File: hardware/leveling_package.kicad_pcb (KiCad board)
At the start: 2 copper layers, 100 x 100 mm, 20 parts, among them J1 Conn_01x16_Male, J2 Conn_01x16_Male, J3 Conn_01x16_Male, J4 Conn_01x16_Male, Q1 BSS138, SW1 SW_Push

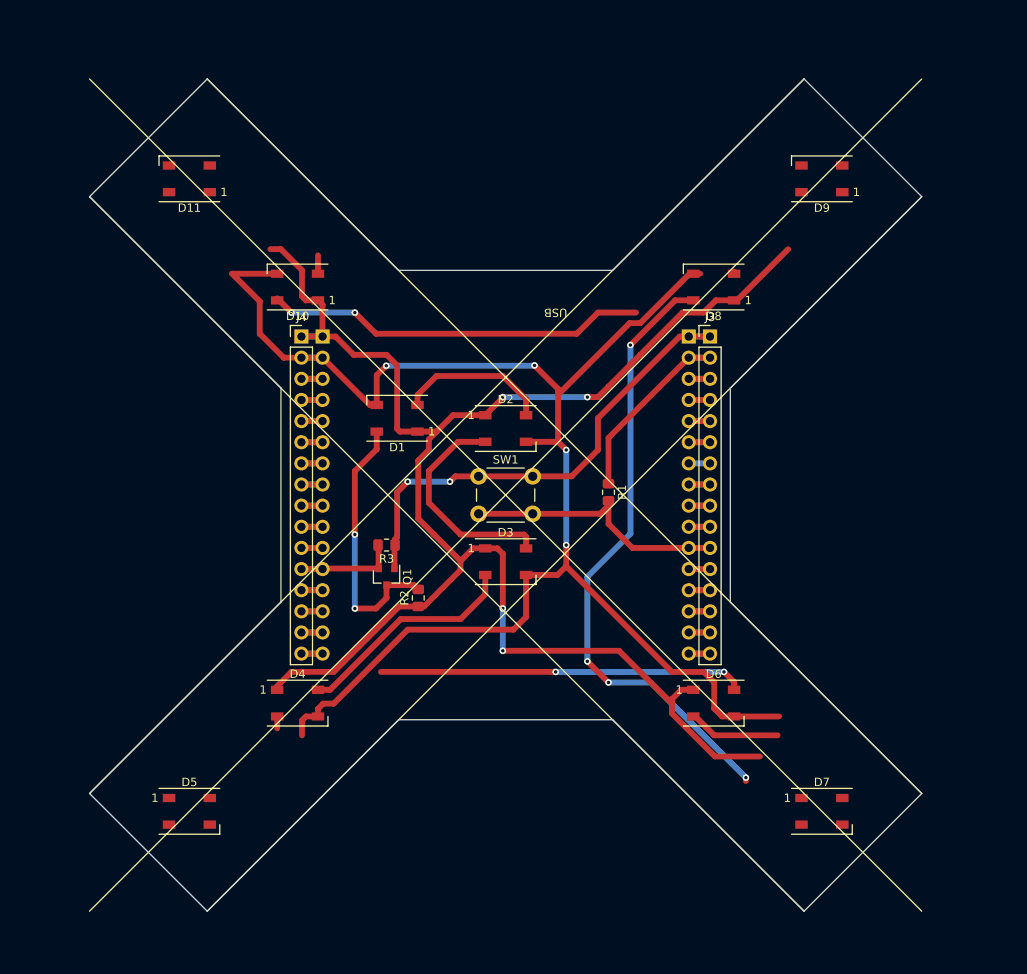
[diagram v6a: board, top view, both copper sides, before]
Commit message: all traces routed
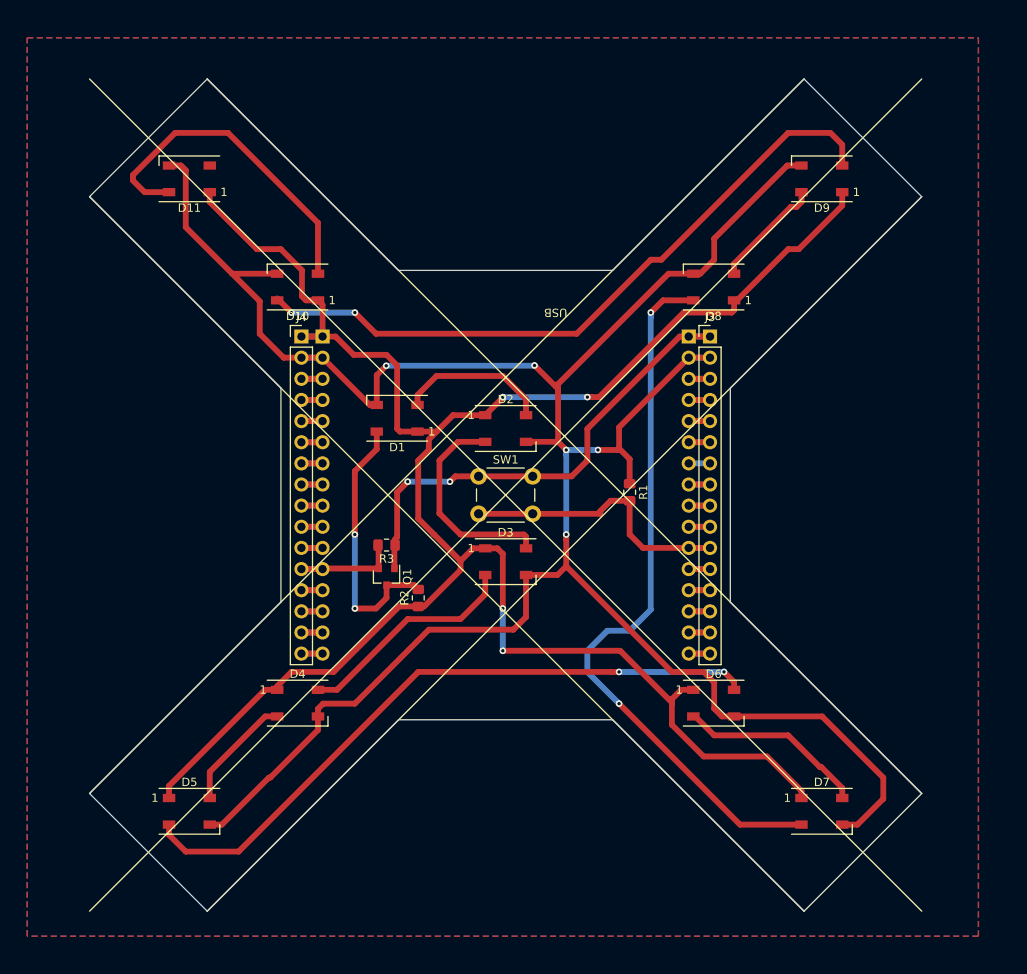
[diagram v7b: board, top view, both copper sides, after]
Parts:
- moved R1 2.54 mm to (88.9, 73.7)
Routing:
- net Net-(D1-Pad3): track 213.7 -> 296.6 mm, vias 4 -> 5
- net Net-(D1-Pad1): track 200.8 -> 250.2 mm
- net Net-(D10-Pad2): track 2.21 -> 40.5 mm
- net Net-(D10-Pad4): track 46.1 -> 82.9 mm
- net Net-(D5-Pad2): track 44.0 -> 80.5 mm
- net Net-(D8-Pad2): track 0.26 -> 13.8 mm
- net Net-(D4-Pad2): track 1.44 -> 14.0 mm
- net Net-(D7-Pad2): track 75.2 -> 87.0 mm, vias 4 -> 2
- net Net-(D6-Pad2): track 11.1 -> 22.7 mm
- net Net-(D2-Pad2): track 26.8 -> 25.8 mm
- net Net-(J1-Pad11): track 35.3 -> 35.9 mm
- added copper zone on B.Cu, net Net-(D1-Pad3)
- added copper zone on F.Cu, net Net-(D1-Pad3)

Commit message: minor corrections
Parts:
- moved D1 2.54 mm to (58.4, 64.8)
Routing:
- net Net-(D1-Pad2): track 18.3 -> 19.7 mm
- net Net-(D1-Pad3): track 296.6 -> 295.2 mm
- net Net-(D1-Pad4): track 32.2 -> 31.2 mm
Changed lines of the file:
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@@
   )
   (module LED_SMD:LED_WS2812B_PLCC4_5.0x5.0mm_P3.2mm (layer F.Cu)
-    (at 60.96 64.77 180)
+    (at 58.42 64.77 180)
     (descr https://cdn-shop.adafruit.com/datasheets/WS2812B.pdf)
     (tags "LED RGB NeoPixel")
@@
   (segment (start 67.68 64.4) (end 71.55 64.4) (width 0.7) (layer F.Cu) (net 30))
   (segment (start 65.71 66.37) (end 67.68 64.4) (width 0.7) (layer F.Cu) (net 30))
-  (segment (start 63.41 66.37) (end 65.71 66.37) (width 0.7) (layer F.Cu) (net 30))
   (segment (start 46.11 97.4) (end 46.55 97.4) (width 0.7) (layer F.Cu) (net 30))
   (segment (start 48.26 95.25) (end 46.55 96.96) (width 0.7) (layer F.Cu) (net 30))
@@
   (segment (start 101.45 50.6) (end 101.45 51.8) (width 0.7) (layer F.Cu) (net 30))
   (segment (start 53.55 54.95) (end 52 54.95) (width 0.7) (layer F.Cu) (net 30))
-  (segment (start 55.75 57.15) (end 53.55 54.95) (width 0.7) (layer F.Cu) (net 30))
-  (segment (start 59.69 57.15) (end 55.75 57.15) (width 0.7) (layer F.Cu) (net 30))
-  (segment (start 60.96 58.42) (end 59.69 57.15) (width 0.7) (layer F.Cu) (net 30))
-  (segment (start 60.96 66.04) (end 60.96 58.42) (width 0.7) (layer F.Cu) (net 30))
-  (segment (start 61.29 66.37) (end 60.96 66.04) (width 0.7) (layer F.Cu) (net 30))
-  (segment (start 63.41 66.37) (end 61.29 66.37) (width 0.7) (layer F.Cu) (net 30))
-  (segment (start 63.41 61.97) (end 65.69 59.69) (width 0.7) (layer F.Cu) (net 31))
-  (segment (start 63.41 63.17) (end 63.41 61.97) (width 0.7) (layer F.Cu) (net 31))
-  (segment (start 65.69 59.69) (end 73.66 59.69) (width 0.7) (layer F.Cu) (net 31))
+  (segment (start 54.48 55.88) (end 53.55 54.95) (width 0.7) (layer F.Cu) (net 30))
+  (segment (start 57.15 55.88) (end 54.48 55.88) (width 0.7) (layer F.Cu) (net 30))
+  (segment (start 58.42 57.15) (end 57.15 55.88) (width 0.7) (layer F.Cu) (net 30))
+  (segment (start 58.42 66.04) (end 58.42 57.15) (width 0.7) (layer F.Cu) (net 30))
+  (segment (start 58.75 66.37) (end 58.42 66.04) (width 0.7) (layer F.Cu) (net 30))
+  (segment (start 60.87 66.37) (end 58.75 66.37) (width 0.7) (layer F.Cu) (net 30))
+  (segment (start 63.83 66.37) (end 64.77 67.31) (width 0.7) (layer F.Cu) (net 30))
+  (segment (start 60.87 66.37) (end 63.83 66.37) (width 0.7) (layer F.Cu) (net 30))
   (segment (start 76.45 62.48) (end 76.45 64.4) (width 0.7) (layer F.Cu) (net 31))
-  (segment (start 73.66 59.69) (end 76.45 62.48) (width 0.7) (layer F.Cu) (net 31))
+  (segment (start 74.93 60.96) (end 76.45 62.48) (width 0.7) (layer F.Cu) (net 31))
+  (segment (start 60.87 61.97) (end 61.88 60.96) (width 0.7) (layer F.Cu) (net 31))
+  (segment (start 60.87 63.17) (end 60.87 61.97) (width 0.7) (layer F.Cu) (net 31))
+  (segment (start 61.88 60.96) (end 74.93 60.96) (width 0.7) (layer F.Cu) (net 31))
   (segment (start 62.985 84.82) (end 63.5 85.335) (width 0.7) (layer F.Cu) (net 32))
   (segment (start 59.69 84.82) (end 62.985 84.82) (width 0.7) (layer F.Cu) (net 32))
@@
   (via (at 55.88 78.74) (size 0.8) (drill 0.4) (layers F.Cu B.Cu) (net 32))
   (segment (start 55.88 87.63) (end 55.88 78.74) (width 0.7) (layer B.Cu) (net 32))
-  (segment (start 55.88 78.74) (end 55.88 71.12) (width 0.7) (layer F.Cu) (net 32))
-  (segment (start 58.51 68.49) (end 58.51 66.37) (width 0.7) (layer F.Cu) (net 32))
-  (segment (start 55.88 71.12) (end 58.51 68.49) (width 0.7) (layer F.Cu) (net 32))
+  (segment (start 55.88 66.46) (end 55.97 66.37) (width 0.7) (layer F.Cu) (net 32))
+  (segment (start 55.88 78.74) (end 55.88 66.46) (width 0.7) (layer F.Cu) (net 32))
   (via (at 81.28 68.58) (size 0.8) (drill 0.4) (layers F.Cu B.Cu) (net 33))
   (segment (start 80.3 67.6) (end 81.28 68.58) (width 0.7) (layer F.Cu) (net 33))
@@
   (segment (start 46.55 47.4) (end 41.142116 47.4) (width 0.7) (layer F.Cu) (net 33))
   (segment (start 44.45 50.707884) (end 41.142116 47.4) (width 0.7) (layer F.Cu) (net 33))
-  (segment (start 57.68 63.17) (end 58.51 63.17) (width 0.7) (layer F.Cu) (net 33))
-  (segment (start 52 57.49) (end 57.68 63.17) (width 0.7) (layer F.Cu) (net 33))
   (segment (start 80.3 61.94) (end 80.3 67.6) (width 0.7) (layer F.Cu) (net 33))
-  (via (at 59.653248 58.456752) (size 0.8) (drill 0.4) (layers F.Cu B.Cu) (net 33))
-  (segment (start 58.51 59.6) (end 59.653248 58.456752) (width 0.7) (layer F.Cu) (net 33))
-  (segment (start 58.51 63.17) (end 58.51 59.6) (width 0.7) (layer F.Cu) (net 33))
   (via (at 77.47 58.42) (size 0.8) (drill 0.4) (layers F.Cu B.Cu) (net 33))
-  (segment (start 77.433248 58.456752) (end 77.47 58.42) (width 0.7) (layer B.Cu) (net 33))
-  (segment (start 59.653248 58.456752) (end 77.433248 58.456752) (width 0.7) (layer B.Cu) (net 33))
   (segment (start 80.3 61.25) (end 80.3 61.94) (width 0.7) (layer F.Cu) (net 33))
   (segment (start 77.47 58.42) (end 80.3 61.25) (width 0.7) (layer F.Cu) (net 33))
@@
   (segment (start 87.45 68.58) (end 87.63 68.4) (width 0.7) (layer F.Cu) (net 33))
   (segment (start 85.09 68.58) (end 87.45 68.58) (width 0.7) (layer F.Cu) (net 33))
+  (segment (start 77.47 58.42) (end 57.15 58.42) (width 0.7) (layer B.Cu) (net 33))
+  (via (at 57.15 58.42) (size 0.8) (drill 0.4) (layers F.Cu B.Cu) (net 33))
+  (segment (start 55.97 59.6) (end 57.15 58.42) (width 0.7) (layer F.Cu) (net 33))
+  (segment (start 55.97 63.17) (end 55.97 59.6) (width 0.7) (layer F.Cu) (net 33))
+  (segment (start 55.312081 59.6) (end 55.97 59.6) (width 0.7) (layer F.Cu) (net 33))
+  (segment (start 53.202081 57.49) (end 55.312081 59.6) (width 0.7) (layer F.Cu) (net 33))
+  (segment (start 52 57.49) (end 53.202081 57.49) (width 0.7) (layer F.Cu) (net 33))
   (segment (start 68.29 67.6) (end 71.55 67.6) (width 0.7) (layer F.Cu) (net 34))
   (segment (start 66.04 76.2) (end 66.04 69.85) (width 0.7) (layer F.Cu) (net 34))
@@
     (polygon
       (pts
-        (xy 130.81 127) (xy 16.51 127) (xy 16.51 19.05) (xy 130.81 19.05)
+        (xy 132.08 127) (xy 17.78 127) (xy 17.78 19.05) (xy 132.08 19.05)
       )
     )
@@
     (polygon
       (pts
-        (xy 130.81 127) (xy 16.51 127) (xy 16.51 19.05) (xy 130.81 19.05)
+        (xy 134.62 129.54) (xy 15.24 129.54) (xy 15.24 16.51) (xy 134.62 16.51)
       )
     )
